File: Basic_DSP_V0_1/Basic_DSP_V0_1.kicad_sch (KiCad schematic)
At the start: 7 parts, among them J13 USB_C_Receptacle

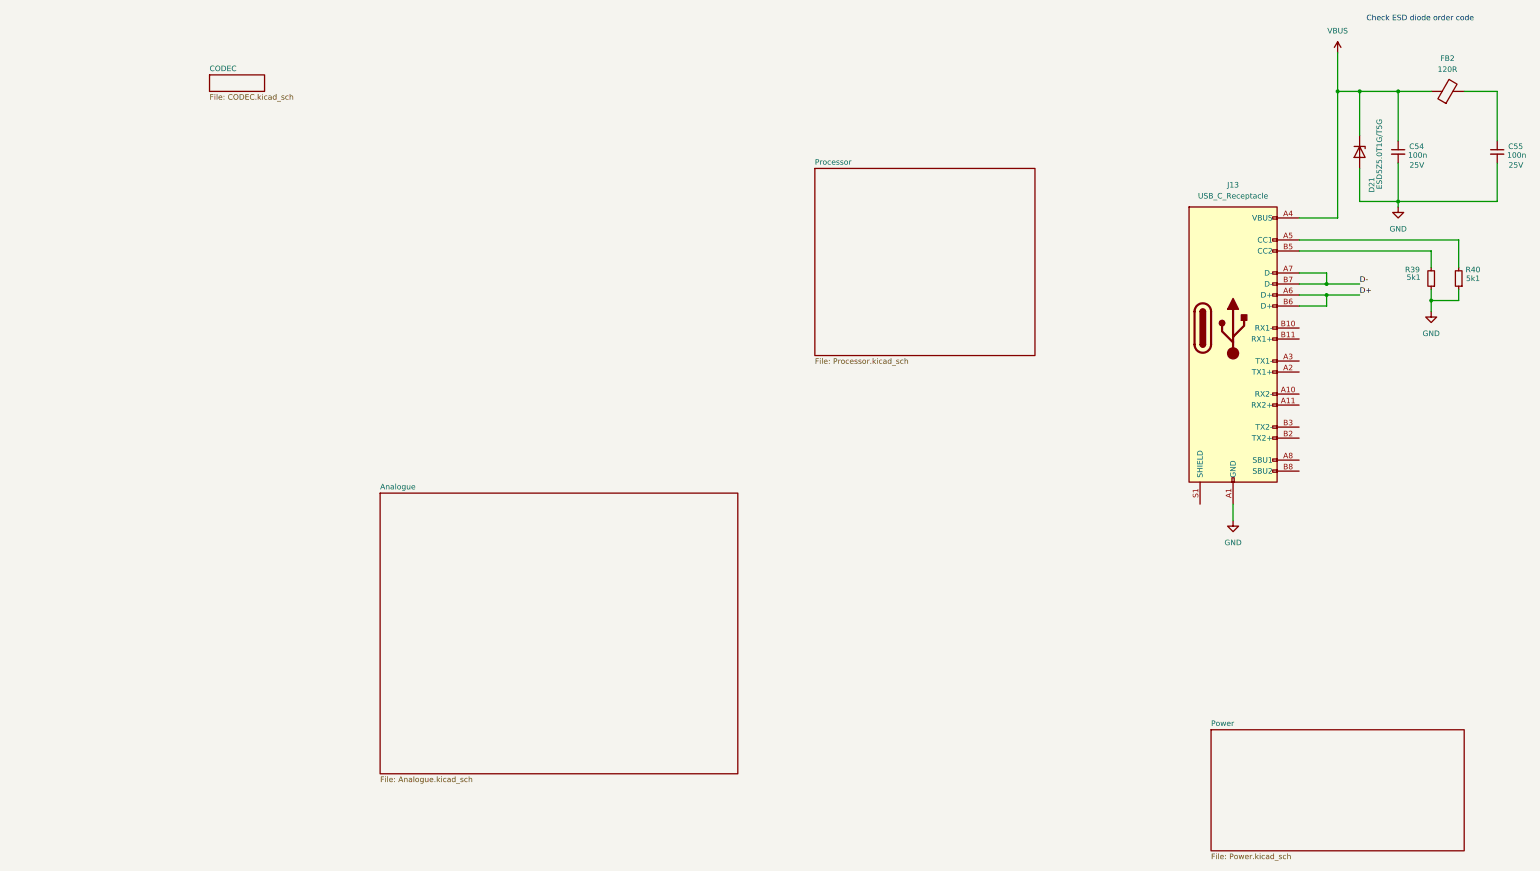
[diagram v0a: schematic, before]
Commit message: Updates to basic DSP schematic
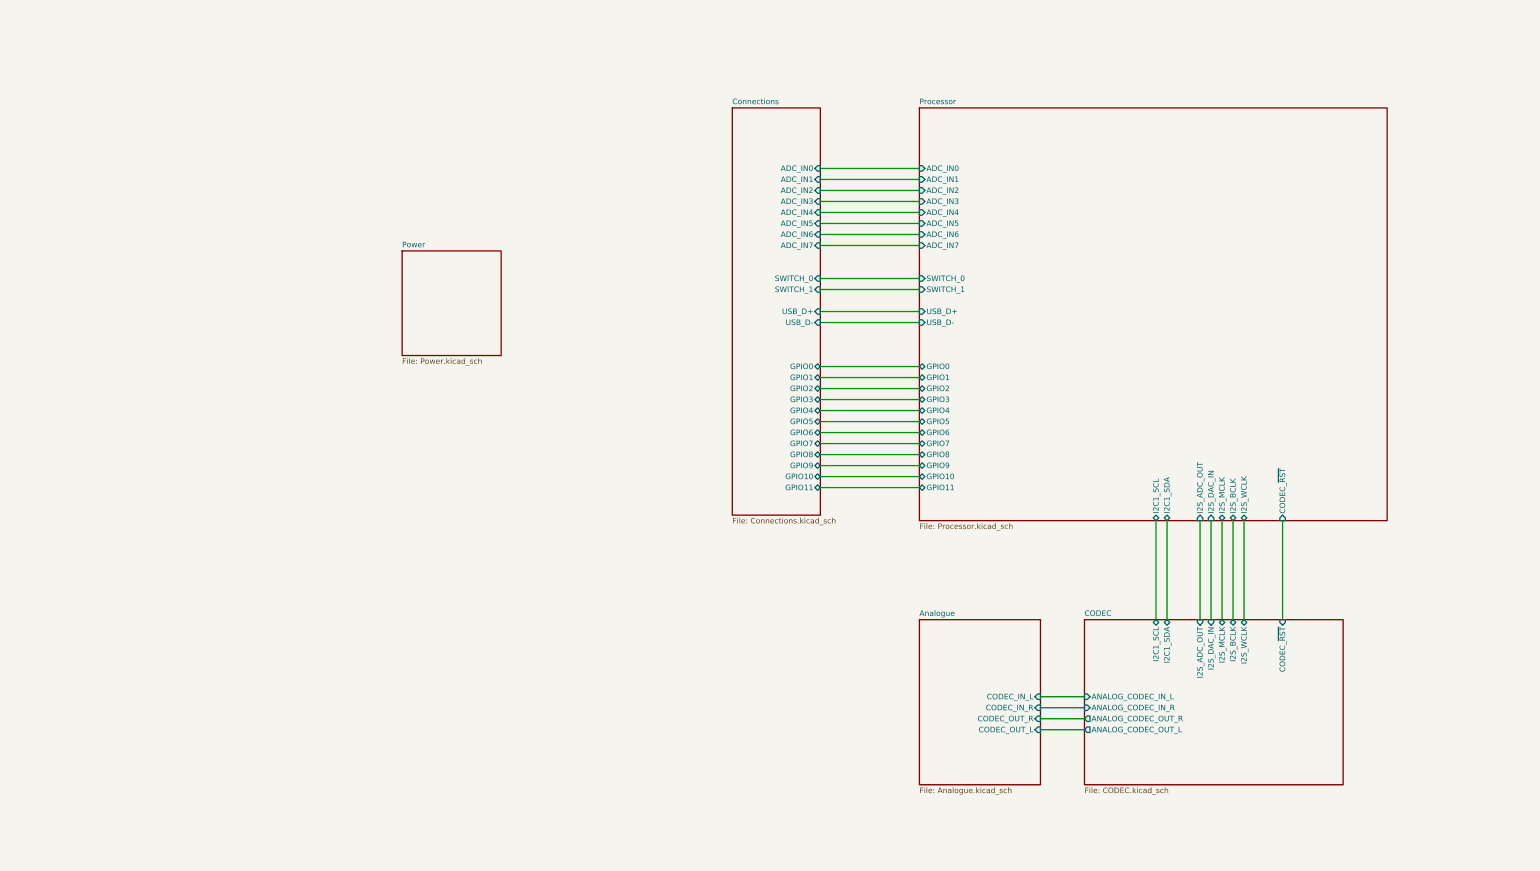
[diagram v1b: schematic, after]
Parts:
- removed C54, C55: 100n, Capacitor_SMD:C_0402_1005Metric, symbol Device:C_Small
- removed D21: ESD5Z5.0T1G/T5G, Diode_SMD:D_SOD-523, symbol Diode:ESD5Zxx
- removed FB2: 120R, Inductor_SMD:L_0603_1608Metric, symbol Device:FerriteBead
- removed J13: USB_C_Receptacle, Connector_USB:USB_C_Receptacle_Molex_105450-0101, symbol Connector:USB_C_Receptacle
- removed R39, R40: 5k1, Resistor_SMD:R_0402_1005Metric_Pad0.72x0.64mm_HandSolder, symbol Device:R_Small
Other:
- added sheet Connections (Connections.kicad_sch)
- sheet Analogue ports: added CODEC_IN_L, CODEC_IN_R, CODEC_OUT_L, CODEC_OUT_R; removed none
- sheet CODEC ports: added ANALOG_CODEC_IN_L, ANALOG_CODEC_IN_R, ANALOG_CODEC_OUT_L, ANALOG_CODEC_OUT_R, CODEC_~{RST}, I2C1_SCL, I2C1_SDA, I2S_ADC_OUT, I2S_BCLK, I2S_DAC_IN, I2S_MCLK, I2S_WCLK; removed none
- sheet Processor ports: added ADC_IN0, ADC_IN1, ADC_IN2, ADC_IN3, ADC_IN4, ADC_IN5, ADC_IN6, ADC_IN7, CODEC_~{RST}, GPIO0, GPIO1, GPIO10, GPIO11, GPIO2, GPIO3, GPIO4, GPIO5, GPIO6, GPIO7, GPIO8, GPIO9, I2C1_SCL, I2C1_SDA, I2S_ADC_OUT, I2S_BCLK, I2S_DAC_IN, I2S_MCLK, I2S_WCLK, SWITCH_0, SWITCH_1, USB_D+, USB_D-; removed none
- note removed: "Check ESD diode order code"

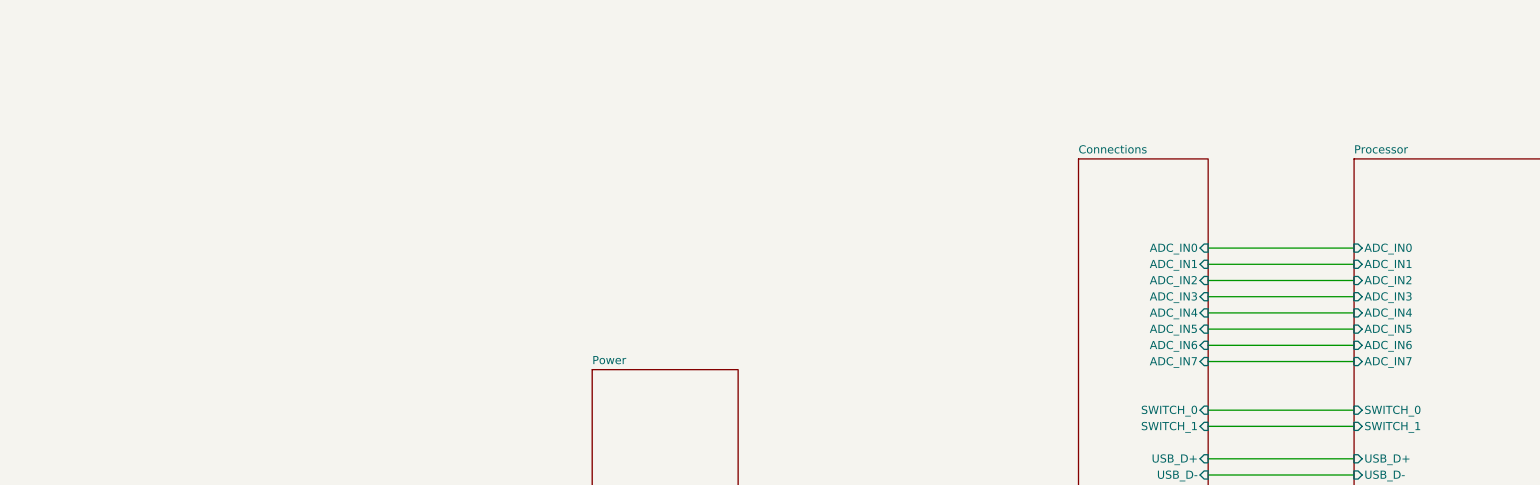
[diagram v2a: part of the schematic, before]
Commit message: Updated parts with LCSC order codes
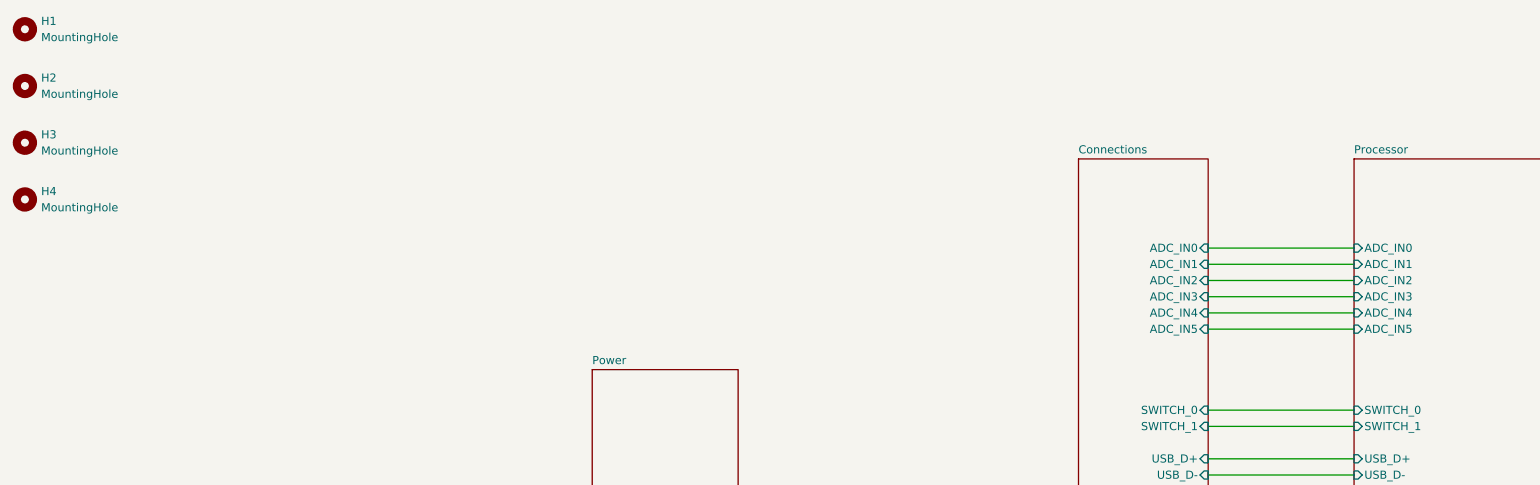
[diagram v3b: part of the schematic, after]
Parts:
- added H1, H2, H3, H4: MountingHole, MountingHole:MountingHole_3.2mm_M3, symbol Mechanical:MountingHole
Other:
- sheet Connections ports: added none; removed ADC_IN6, ADC_IN7
- sheet Processor ports: added none; removed ADC_IN6, ADC_IN7

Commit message: No errors from DRC on layout
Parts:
- H1, H2, H3, H4: footprint MountingHole:MountingHole_3.2mm_M3 -> MountingHole:MountingHole_3.2mm_M3_ISO7380_Pad
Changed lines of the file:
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@@
 			)
 		)
-		(property "Footprint" "MountingHole:MountingHole_3.2mm_M3"
+		(property "Footprint" "MountingHole:MountingHole_3.2mm_M3_ISO7380_Pad"
 			(at 33.02 45.72 0)
 			(effects
@@
 			)
 		)
-		(property "Footprint" "MountingHole:MountingHole_3.2mm_M3"
+		(property "Footprint" "MountingHole:MountingHole_3.2mm_M3_ISO7380_Pad"
 			(at 33.02 54.61 0)
 			(effects
@@
 			)
 		)
-		(property "Footprint" "MountingHole:MountingHole_3.2mm_M3"
+		(property "Footprint" "MountingHole:MountingHole_3.2mm_M3_ISO7380_Pad"
 			(at 33.02 72.39 0)
 			(effects
@@
 			)
 		)
-		(property "Footprint" "MountingHole:MountingHole_3.2mm_M3"
+		(property "Footprint" "MountingHole:MountingHole_3.2mm_M3_ISO7380_Pad"
 			(at 33.02 63.5 0)
 			(effects
